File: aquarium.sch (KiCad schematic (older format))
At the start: 39 parts, among them U1 MOC3063, U2 MOC3063

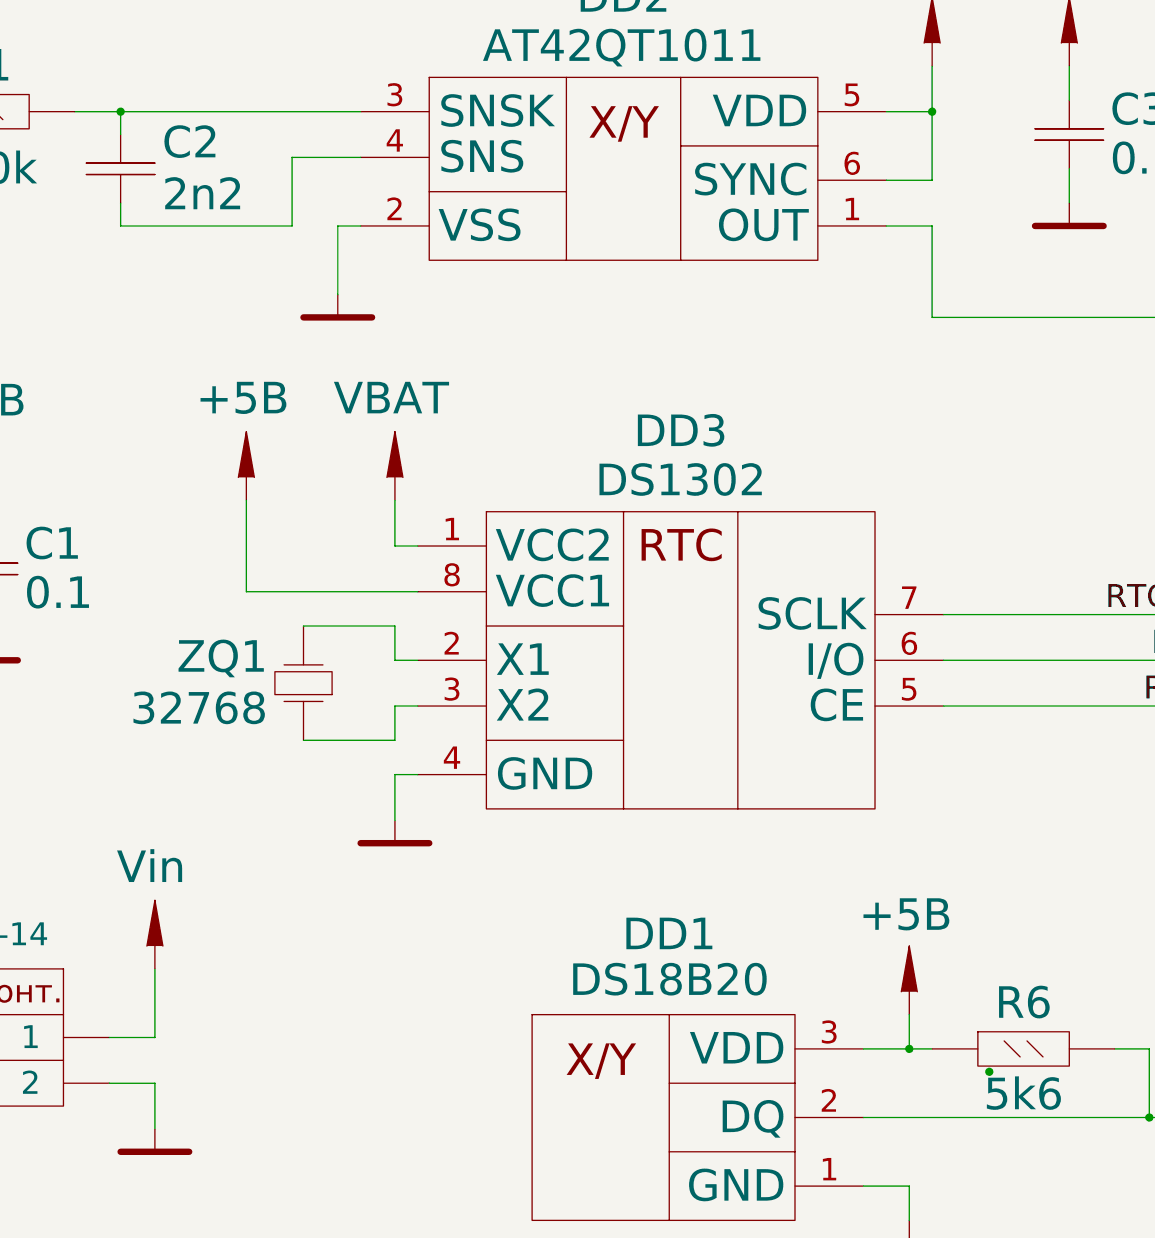
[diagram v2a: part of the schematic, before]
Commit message: Changed capacity of the reference capacitor of the sensor IC. Corrected initialization of the time correction variable.
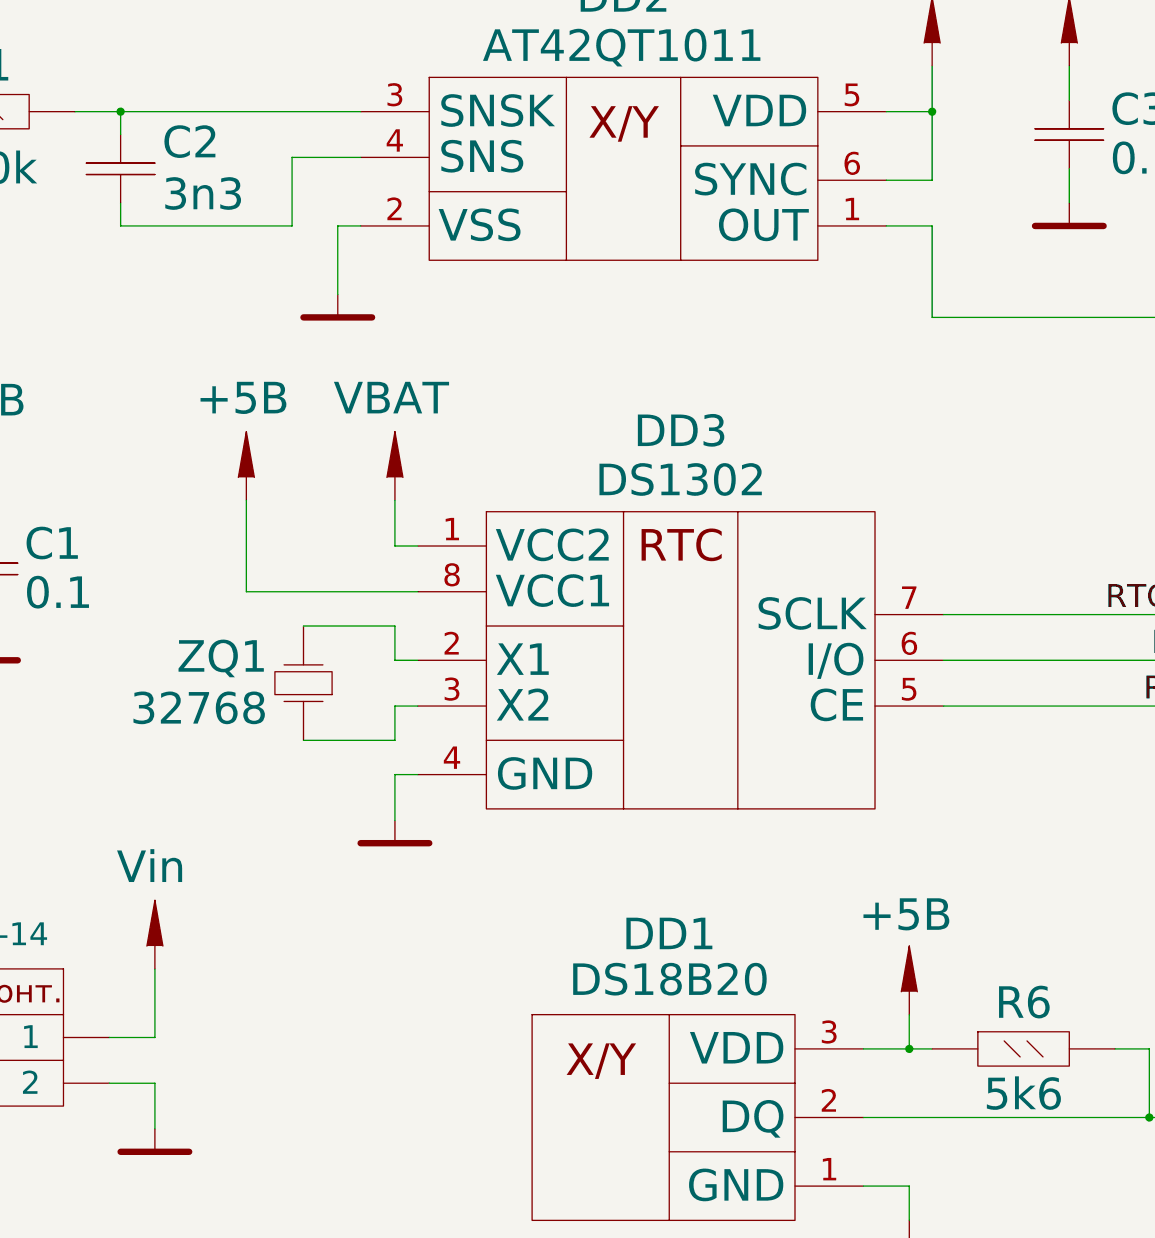
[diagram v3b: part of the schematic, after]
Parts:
- C2: value 2n2 -> 3n3
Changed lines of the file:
@@
 P 2750 1950
 F 0 "C2" H 2931 2064 138 0000 L CNN
-F 1 "2n2" H 2931 1837 138 0000 L CNN
+F 1 "3n3" H 2931 1837 138 0000 L CNN
 F 2 "Конденсаторы:SMD_0805" H 2750 1975 60  0001 C CNN
 F 3 "" H 2750 1975 60  0000 C CNN
@@
 Wire Wire Line
 	9350 8350 9350 8800
-Connection ~ 6550 5900
 Connection ~ 8550 4100
 $EndSCHEMATC

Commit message: New version of the controller (schematic and pcb).
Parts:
- removed C4, C7: 0.1, Конденсаторы:SMD_0805, symbol C
- removed DA1: 78L05, Транзисторы:TO92-250, symbol 78L05
- removed R2, R3, R4, R5: 360, Резисторы:RH_2, symbol R2
- removed R7: 620, Резисторы:R_0805, symbol R.125
- removed U1, U2: MOC3063, Микросхемы:DIP6-300, symbol MOC3063
- removed VS1, VS2: BT137, Транзисторы:TO220, symbol BT137
- removed XT1, XT2, XT3: DG350-3.5-02P-14, Разъемы:DG-350-2, symbol 282844-2
- added C2, C3: 0.1, Конденсаторы:SMD_0805, symbol C
- added C6: 3n3, Конденсаторы:SMD_0805, symbol C
- added DD3: AT42QT1011, Транзисторы:SOT23-6, symbol AT42QT1011
- added R4: 30, Резисторы:R_0805, symbol R.125
- added VT1: IRLD014, Транзисторы:HVMDIP, symbol IRLD014
- added XP2: Sensor 2, Разъемы:PLS-1, symbol Pin
- added XT3: PLS-4, Разъемы:PLS-4, symbol PLS-4
- GB1: value 3V -> 3В
- R8: value 620 -> 100k
- XP1: value Sensor -> Sensor 1
- XT2: renamed from XT6; value PLD-6 -> PLS-6; footprint Разъемы:PLD-6 -> Разъемы:PLS-6
- ZQ1: footprint Резисторы:R_0805 -> Прочее:HC_3.0x8.0mm
- renumbered C3 to C1, C5 to C4, C2 to C5, C6 to C7, C1 to C9, DD4 to DD1, DD3 to DD4, DD1 to DD5, R12 to R1, R11 to R2, R10 to R3, R9 to R5, R1 to R7, XT5 to XT1
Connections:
- net +5B: now also DD4.1 (VCC2), XT3.2; no longer C1.1, C8.1, DD2.5 (VDD), DD2.6 (SYNC), DD4.8 (VCC1), DD5.3 (VDD), R6.1
- net A: now also DD1.2 (PD4); no longer DD1.14 (PB2)
- net B: now also DD1.32 (PD2); no longer DD1.10 (PD6)
- net C: now also DD1.11 (PD7); no longer DD1.25 (PC2)
- net D: now also DD1.9 (PD5); no longer DD1.17 (PB5), XT2.3
- net DGT1: now also DD1.26 (PC3); no longer DD1.15 (PB3), XT2.4
- net DGT2: now also DD1.27 (PC4); no longer DD1.12 (PB0)
- net DGT3: now also DD1.28 (PC5); no longer DD1.11 (PD7)
- net DGT4: now also DD1.13 (PB1); no longer DD1.23 (PC0)
- net E: now also DD1.8 (PB7); no longer DD1.16 (PB4), XT2.1
- net F: now also DD1.1 (PD3); no longer DD1.13 (PB1)
- net G: now also DD1.12 (PB0); no longer DD1.24 (PC1)
- net GND: now also XT1.2, XT2.3, C2.2, C3.2, DD3.2 (VSS), VT1.3 (S), XT3.3; no longer XT1.4, XT2.6
- net H: now also DD1.10 (PD6); no longer DD1.26 (PC3)
- net HEAT: now also DD1.7 (PB6), XT3.4; no longer DD1.28 (PC5)
- net LIGHT: now also DD1.14 (PB2), R4.1; no longer DD1.27 (PC4), R8.2
- net RTC_IO: now also DD1.17 (PB5), XT2.5; no longer DD1.8 (PB7)
- net TEMP: now also DD1.25 (PC2), R6.1; no longer DD1.1 (PD3), R6.2
- net TX: now also XT1.4; no longer XT1.2
- net ~RESET: now also C8.1, XT2.1; no longer XT2.5
- net SENS_1: now reaches DD1.19 (ADC6)
- net SENS_1: now also DD2.1 (OUT)
- net SENS_2: now reaches DD1.22 (ADC7)
- net SENS_2: now also DD3.1 (OUT)
- net at R8.1: now also XP2.1
- net +12B: now reaches XT4.1
- net +12B: now also XT3.1
- net at XT4.2: now also VT1.1 (D)
- net RTC_CE renamed MISO
- net MISO: now also DD1.16 (PB4), XT2.4; no longer DD1.9 (PD5)
- net RTC_SCLK renamed MOSI
- net MOSI: now also DD1.15 (PB3), XT2.6; no longer DD1.7 (PB6)
- removed net SENS: DD1.2 (PD4), DD2.1 (OUT)
- net VBAT: no longer names the net of GB1.1 (+)
- net VBAT: now also DD4.8 (VCC1); no longer DD4.1 (VCC2)
- new net: R4.2, VT1.2 (G)
- new net: C6.1, DD3.3 (SNSK), R8.2
- new net: C6.2, DD3.4 (SNS)
- new net SENS_PWR: C1.1, C2.1, DD1.23 (PC0), DD2.5 (VDD), DD2.6 (SYNC), DD3.5 (VDD), DD3.6 (SYNC)
- new net TEMP_PWR: C3.1, DD1.24 (PC1), DD5.3 (VDD), R6.2
- no-connect marks 3 -> 0
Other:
- note added: "+12В"
- note added: "PICkit2"
- note added: "POWER"
- note added: "Общ."
- note added: "Свет (+)"
- note added: "Свет (-)"
- note added: "Упр. нагр."
- note removed: "ISP6"
- note removed: "~~220В"
- note removed: "Нагрев."
- note removed: "Общий"
- note removed: "Свет"
- moved on the sheet: C1, C4, C5, C7, C9, DD1, DD2, DD4, DD5, HG1, R1, R2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

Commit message: Finished working on PCB.
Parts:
- ZQ1: Тип (none) -> 6пФ
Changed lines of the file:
@@
 F 2 "Прочее:HC_3.0x8.0mm" H 9100 10450 60  0001 C CNN
 F 3 "" H 9100 10450 60  0000 C CNN
+F 4 "6пФ" V 8775 10300 138 0000 R CNN "Тип"
 	1    9100 10450
 	0    -1   -1   0

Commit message: New version of the schematic and PCB's.
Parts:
- added C18*: 0.33, Конденсаторы:SMD_0805, symbol C
- added R18: 470, Резисторы:R_0805, symbol R.125
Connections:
- net GND: now also C18*.2
- net RTC_IO: now also R18.2; no longer DD4.6 (I/O)
- net at DD4.8 (VCC1), GB1.1 (+): now also C18*.1
- new net: DD4.6 (I/O), R18.1
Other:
- moved on the sheet: C9
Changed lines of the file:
@@
 $EndComp
 $Comp
-L GND #PWR01
+L GND #PWR17
 U 1 1 56791BEA
 P 9500 1550
-F 0 "#PWR01" H 9900 1550 138 0001 C CNN
+F 0 "#PWR17" H 9900 1550 138 0001 C CNN
 F 1 "GND" H 9150 1550 138 0001 C CNN
 F 2 "" H 9500 1550 60  0000 C CNN
@@
 $EndComp
 $Comp
-L GND #PWR02
+L GND #PWR19
 U 1 1 56791C0B
 P 10200 1550
-F 0 "#PWR02" H 10600 1550 138 0001 C CNN
+F 0 "#PWR19" H 10600 1550 138 0001 C CNN
 F 1 "GND" H 9850 1550 138 0001 C CNN
 F 2 "" H 10200 1550 60  0000 C CNN
@@
 $EndComp
 $Comp
-L +5B #PWR03
+L +5B #PWR16
 U 1 1 56791C40
 P 9500 750
-F 0 "#PWR03" H 10000 850 138 0001 C CNN
+F 0 "#PWR16" H 10000 850 138 0001 C CNN
 F 1 "+5B" H 9484 1185 138 0000 C CNN
 F 2 "" H 9500 950 60  0000 C CNN
@@
 $EndComp
 $Comp
-L +5B #PWR04
+L +5B #PWR18
 U 1 1 56791C61
 P 10200 750
-F 0 "#PWR04" H 10700 850 138 0001 C CNN
+F 0 "#PWR18" H 10700 850 138 0001 C CNN
 F 1 "+5B" H 10184 1185 138 0000 C CNN
 F 2 "" H 10200 950 60  0000 C CNN
@@
 	10200 1300 10200 1550
 $Comp
-L +5B #PWR05
+L +5B #PWR14
 U 1 1 56791F4C
 P 8750 750
-F 0 "#PWR05" H 9250 850 138 0001 C CNN
+F 0 "#PWR14" H 9250 850 138 0001 C CNN
 F 1 "+5B" H 8734 1185 138 0000 C CNN
 F 2 "" H 8750 950 60  0000 C CNN
@@
 Connection ~ 8750 950
 $Comp
-L GND #PWR06
+L GND #PWR15
 U 1 1 567920EA
 P 8750 4550
-F 0 "#PWR06" H 9150 4550 138 0001 C CNN
+F 0 "#PWR15" H 9150 4550 138 0001 C CNN
 F 1 "GND" H 8400 4550 138 0001 C CNN
 F 2 "" H 8750 4550 60  0000 C CNN
@@
 $EndComp
 $Comp
-L GND #PWR07
+L GND #PWR6
 U 1 1 56795326
 P 5350 6250
-F 0 "#PWR07" H 5750 6250 138 0001 C CNN
+F 0 "#PWR6" H 5750 6250 138 0001 C CNN
 F 1 "GND" H 5000 6250 138 0001 C CNN
 F 2 "" H 5350 6250 60  0000 C CNN
@@
 L C C9
 U 1 1 5679539A
-P 11100 10450
-F 0 "C9" H 11278 10558 138 0000 L CNN
-F 1 "0.1" H 11278 10343 138 0000 L CNN
-F 2 "Конденсаторы:SMD_0805" H 11100 10475 60  0001 C CNN
-F 3 "" H 11100 10475 60  0000 C CNN
-	1    11100 10450
-	1    0    0    -1
-$EndComp
-$Comp
-L GND #PWR08
+P 11000 12600
+F 0 "C9" H 11178 12708 138 0000 L CNN
+F 1 "0.1" H 11178 12493 138 0000 L CNN
+F 2 "Конденсаторы:SMD_0805" H 11000 12625 60  0001 C CNN
+F 3 "" H 11000 12625 60  0000 C CNN
+	1    11000 12600
+	1    0    0    -1
+$EndComp
+$Comp
+L GND #PWR24
 U 1 1 567953A0
-P 11100 11050
-F 0 "#PWR08" H 11500 11050 138 0001 C CNN
-F 1 "GND" H 10750 11050 138 0001 C CNN
-F 2 "" H 11100 11050 60  0000 C CNN
-F 3 "" H 11100 11050 60  0000 C CNN
-	1    11100 11050
-	-1   0    0    -1
-$EndComp
-$Comp
-L +5B #PWR09
+P 11000 13200
+F 0 "#PWR24" H 11400 13200 138 0001 C CNN
+F 1 "GND" H 10650 13200 138 0001 C CNN
+F 2 "" H 11000 13200 60  0000 C CNN
+F 3 "" H 11000 13200 60  0000 C CNN
+	1    11000 13200
+	-1   0    0    -1
+$EndComp
+$Comp
+L +5B #PWR23
 U 1 1 567953A6
-P 11100 10000
-F 0 "#PWR09" H 11600 10100 138 0001 C CNN
-F 1 "+5B" H 11084 10435 138 0000 C CNN
-F 2 "" H 11100 10200 60  0000 C CNN
-F 3 "" H 11100 10200 60  0000 C CNN
-	1    11100 10000
-	-1   0    0    -1
-$EndComp
-Wire Wire Line
-	11100 10000 11100 10300
-Wire Wire Line
-	11100 10600 11100 11050
+P 11000 12150
+F 0 "#PWR23" H 11500 12250 138 0001 C CNN
+F 1 "+5B" H 10984 12585 138 0000 C CNN
+F 2 "" H 11000 12350 60  0000 C CNN
+F 3 "" H 11000 12350 60  0000 C CNN
+	1    11000 12150
+	-1   0    0    -1
+$EndComp
+Wire Wire Line
+	11000 12150 11000 12450
+Wire Wire Line
+	11000 12750 11000 13200
 $Comp
 L QUARTZ ZQ1
@@
 	8700 10200 9100 10200
 $Comp
-L +5B #PWR010
+L +5B #PWR11
 U 1 1 56797DB1
 P 8700 9650
-F 0 "#PWR010" H 9200 9750 138 0001 C CNN
+F 0 "#PWR11" H 9200 9750 138 0001 C CNN
 F 1 "+5B" H 8684 10094 138 0000 C CNN
 F 2 "" H 8700 9850 60  0000 C CNN
@@
 	8700 9850 8600 9850
 Wire Wire Line
-	8600 10050 10200 10050
+	8600 10050 11000 10050
 $Comp
 L C C5
@@
 $EndComp
 $Comp
-L GND #PWR011
+L GND #PWR12
 U 1 1 5679847B
 P 8700 11050
-F 0 "#PWR011" H 9100 11050 138 0001 C CNN
+F 0 "#PWR12" H 9100 11050 138 0001 C CNN
 F 1 "GND" H 8350 11050 138 0001 C CNN
 F 2 "" H 8700 11050 60  0000 C CNN
@@
 	9600 6350 9600 6250
 $Comp
-L GND #PWR012
+L GND #PWR9
 U 1 1 56798CBF
 P 8600 6650
-F 0 "#PWR012" H 9000 6650 138 0001 C CNN
+F 0 "#PWR9" H 9000 6650 138 0001 C CNN
 F 1 "GND" H 8250 6650 138 0001 C CNN
 F 2 "" H 8600 6650 60  0000 C CNN
@@
 $EndComp
 $Comp
-L GND #PWR013
+L GND #PWR8
 U 1 1 567A531F
 P 6400 13200
-F 0 "#PWR013" H 6800 13200 138 0001 C CNN
+F 0 "#PWR8" H 6800 13200 138 0001 C CNN
 F 1 "GND" H 6050 13200 138 0001 C CNN
 F 2 "" H 6400 13200 60  0000 C CNN
@@
 GND
 $Comp
-L GND #PWR014
+L GND #PWR2
 U 1 1 567D101C
 P 2000 6100
-F 0 "#PWR014" H 2400 6100 138 0001 C CNN
+F 0 "#PWR2" H 2400 6100 138 0001 C CNN
 F 1 "GND" H 1650 6100 138 0001 C CNN
 F 2 "" H 2000 6100 60  0000 C CNN
@@
 	6300 10150 4300 10150
 Wire Wire Line
-	6300 10350 4300 10350
+	6300 10350 5950 10350
+Wire Wire Line
+	4300 10350 5150 10350
 Entry Wire Line
 	4300 10550 4200 10650
@@
 $EndSheet
 $Comp
-L GND #PWR015
+L GND #PWR20
 U 1 1 58491DD9
 P 10200 11050
-F 0 "#PWR015" H 10600 11050 138 0001 C CNN
+F 0 "#PWR20" H 10600 11050 138 0001 C CNN
 F 1 "GND" H 9850 11050 138 0001 C CNN
 F 2 "" H 10200 11050 60  0000 C CNN
@@
 	2000 11800 2000 11950
 $Comp
-L +5B #PWR016
+L +5B #PWR4
 U 1 1 584B914C
 P 2650 4900
-F 0 "#PWR016" H 3150 5000 138 0001 C CNN
+F 0 "#PWR4" H 3150 5000 138 0001 C CNN
 F 1 "+5B" H 2634 5335 138 0000 C CNN
 F 2 "" H 2650 5100 60  0000 C CNN
@@
 $EndComp
 $Comp
-L GND #PWR017
+L GND #PWR13
 U 1 1 584EFF17
 P 8700 13200
-F 0 "#PWR017" H 9100 13200 138 0001 C CNN
+F 0 "#PWR13" H 9100 13200 138 0001 C CNN
 F 1 "GND" H 8350 13200 138 0001 C CNN
 F 2 "" H 8700 13200 60  0000 C CNN
@@
 Connection ~ 6400 11650
 $Comp
-L +12B #PWR018
+L +12B #PWR1
 U 1 1 58470EC2
 P 2000 4900
-F 0 "#PWR018" H 2500 5000 138 0001 C CNN
+F 0 "#PWR1" H 2500 5000 138 0001 C CNN
 F 1 "+12B" H 1987 5345 138 0000 C CNN
 F 2 "" H 2000 5100 60  0000 C CNN
@@
 	2000 4900 2000 5200
 $Comp
-L +12B #PWR019
+L +12B #PWR5
 U 1 1 586A2E7C
 P 2650 6900
-F 0 "#PWR019" H 3150 7000 138 0001 C CNN
+F 0 "#PWR5" H 3150 7000 138 0001 C CNN
 F 1 "+12B" H 2637 7345 138 0000 C CNN
 F 2 "" H 2650 7100 60  0000 C CNN
@@
 	2000 7400 2000 7700
 $Comp
-L GND #PWR020
+L GND #PWR3
 U 1 1 586A3FC9
 P 2000 8700
-F 0 "#PWR020" H 2400 8700 138 0001 C CNN
+F 0 "#PWR3" H 2400 8700 138 0001 C CNN
 F 1 "GND" H 1650 8700 138 0001 C CNN
 F 2 "" H 2000 8700 60  0000 C CNN
@@
 TEMP_PWR
 Wire Wire Line
-	6000 5350 4300 5350
+	4300 5350 6000 5350
 Entry Wire Line
 	4300 5350 4200 5450
@@
 $EndComp
 $Comp
-L GND #PWR021
+L GND #PWR7
 U 1 1 586F73E8
 P 5350 8200
-F 0 "#PWR021" H 5750 8200 138 0001 C CNN
+F 0 "#PWR7" H 5750 8200 138 0001 C CNN
 F 1 "GND" H 5000 8200 138 0001 C CNN
 F 2 "" H 5350 8200 60  0000 C CNN
@@
 	9600 8300 9600 8200
 $Comp
-L GND #PWR022
+L GND #PWR10
 U 1 1 586F7403
 P 8600 8600
-F 0 "#PWR022" H 9000 8600 138 0001 C CNN
+F 0 "#PWR10" H 9000 8600 138 0001 C CNN
 F 1 "GND" H 8250 8600 138 0001 C CNN
 F 2 "" H 8600 8600 60  0000 C CNN
@@
 SENS_2
 Wire Wire Line
-	6000 7300 4300 7300
+	4300 7300 6000 7300
 Entry Wire Line
 	4300 7300 4200 7400
@@
 $EndComp
 $Comp
-L GND #PWR023
+L GND #PWR21
 U 1 1 586F79F4
 P 10800 1550
-F 0 "#PWR023" H 11200 1550 138 0001 C CNN
+F 0 "#PWR21" H 11200 1550 138 0001 C CNN
 F 1 "GND" H 10450 1550 138 0001 C CNN
 F 2 "" H 10800 1550 60  0000 C CNN
@@
 Connection ~ 5350 5350
 Connection ~ 5350 7300
+$Comp
+L R.125 R18
+U 1 1 58978D6E
+P 5550 10350
+F 0 "R18" H 5550 10700 138 0000 C CNN
+F 1 "470" H 5550 9975 138 0000 C CNN
+F 2 "Резисторы:R_0805" H 5550 10350 60  0001 C CNN
+F 3 "" H 5550 10350 60  0000 C CNN
+	1    5550 10350
+	-1   0    0    -1
+$EndComp
+$Comp
+L C C18*
+U 1 1 58C4168F
+P 11000 10450
+F 0 "C18*" H 11178 10558 138 0000 L CNN
+F 1 "0.33" H 11178 10343 138 0000 L CNN
+F 2 "Конденсаторы:SMD_0805" H 11000 10475 60  0001 C CNN
+F 3 "" H 11000 10475 60  0000 C CNN
+	1    11000 10450
+	1    0    0    -1
+$EndComp
+$Comp
+L GND #PWR22
+U 1 1 58C41695
+P 11000 11050
+F 0 "#PWR22" H 11400 11050 138 0001 C CNN
+F 1 "GND" H 10650 11050 138 0001 C CNN
+F 2 "" H 11000 11050 60  0000 C CNN
+F 3 "" H 11000 11050 60  0000 C CNN
+	1    11000 11050
+	-1   0    0    -1
+$EndComp
+Wire Wire Line
+	11000 10050 11000 10300
+Wire Wire Line
+	11000 10600 11000 11050
+Connection ~ 10200 10050
 $EndSCHEMATC
